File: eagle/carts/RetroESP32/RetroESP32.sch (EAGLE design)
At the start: 13 parts, among them J5 503182-1852_503182-1852, Q4 mmbt2222, Q5 mmbt2222, U1 ESP32-WROVER_ESP32-WROVER

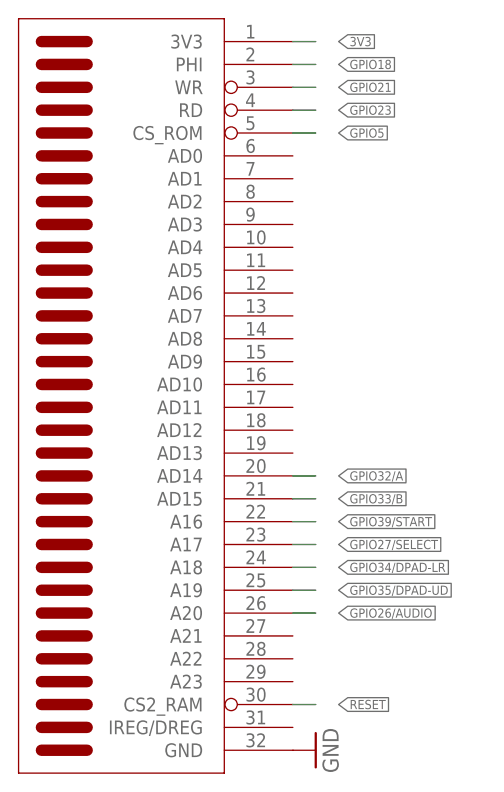
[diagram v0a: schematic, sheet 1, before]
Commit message: feat: update USB and VCC lines on ATMega
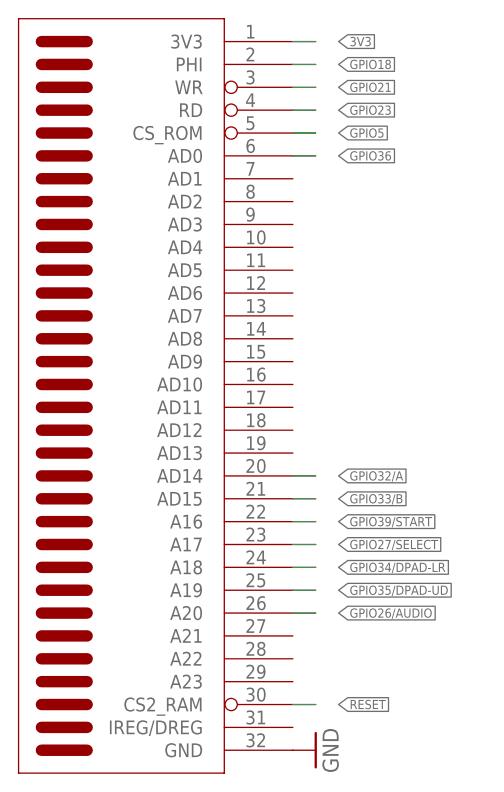
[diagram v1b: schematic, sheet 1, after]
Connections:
- net GPIO36: now also U$2.AD0
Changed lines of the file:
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@@
+</segment>
+</net>
+<net name="GPIO36" class="0">
+<segment>
+<pinref part="U$2" gate="G$1" pin="AD0"/>
+<wire x1="53.34" y1="91.44" x2="55.88" y2="91.44" width="0.1524" layer="91"/>
+<label x="58.42" y="91.44" size="1.016" layer="95" xref="yes"/>
 </segment>
 </net>
